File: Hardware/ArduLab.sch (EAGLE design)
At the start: 92 parts, among them CN1 USB-B, CN2 JST-PH, Q1 BSS138, Q2 BSS138, U1 ATMEGA32U4-AU, U2 MIC5205, U3 PAM2401, U4 MCP73831, U5 L293DD, U6 HC_05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

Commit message: Update
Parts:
- renumbered PB1 to S3, PB2 to S4
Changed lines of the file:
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@@
 <part name="GND32" library="SparkFun" deviceset="GND" device=""/>
 <part name="P+11" library="SparkFun" deviceset="3.3V" device="" value="VCC"/>
-<part name="PB2" library="Testing" deviceset="SWITCH-MOMENTARY-2" device="SMD-4" value="Reset"/>
+<part name="S4" library="Testing" deviceset="SWITCH-MOMENTARY-2" device="SMD-4" value="Reset"/>
 <part name="JP1" library="pinhead" deviceset="PINHD-2X4" device=""/>
 <part name="C16" library="resistor" deviceset="C-US" device="C1206" value="1uF"/>
@@
 <part name="R6" library="resistor" deviceset="R-US_" device="R1206" value="330"/>
 <part name="GND17" library="SparkFun" deviceset="GND" device=""/>
-<part name="PB1" library="SparkFun-Electromechanical" deviceset="SWITCH-MOMENTARY-2" device="SMD-12MM" value="B3FS-4052P"/>
+<part name="S3" library="SparkFun-Electromechanical" deviceset="SWITCH-MOMENTARY-2" device="SMD-12MM" value="B3FS-4052P"/>
 <part name="C23" library="SparkFun" deviceset="CAP_POL" device="3528-KIT" value="100uF"/>
 <part name="C11" library="resistor" deviceset="C-US" device="C1206" value="100nF"/>
@@
 <instance part="GND32" gate="1" x="25.4" y="36.83"/>
 <instance part="P+11" gate="G$1" x="149.86" y="46.99"/>
-<instance part="PB2" gate="G$1" x="149.86" y="20.32" rot="R90"/>
+<instance part="S4" gate="G$1" x="149.86" y="20.32" rot="R90"/>
 <instance part="JP1" gate="A" x="114.3" y="41.91"/>
 <instance part="C16" gate="G$1" x="22.86" y="135.89" rot="R90"/>
@@
 <wire x1="149.86" y1="15.24" x2="149.86" y2="12.7" width="0.1524" layer="91"/>
 <pinref part="GND3" gate="1" pin="GND"/>
-<pinref part="PB2" gate="G$1" pin="1"/>
+<pinref part="S4" gate="G$1" pin="1"/>
 </segment>
 <segment>
@@
 <pinref part="R12" gate="G$1" pin="1"/>
 <wire x1="149.86" y1="25.4" x2="149.86" y2="27.94" width="0.1524" layer="91"/>
-<pinref part="PB2" gate="G$1" pin="2"/>
+<pinref part="S4" gate="G$1" pin="2"/>
 <junction x="149.86" y="27.94"/>
 <wire x1="149.86" y1="27.94" x2="149.86" y2="30.48" width="0.1524" layer="91"/>
@@
 <instance part="R6" gate="G$1" x="35.56" y="149.86" rot="R180"/>
 <instance part="GND17" gate="1" x="20.32" y="139.7"/>
-<instance part="PB1" gate="G$1" x="115.57" y="64.77" rot="R270"/>
+<instance part="S3" gate="G$1" x="115.57" y="64.77" rot="R270"/>
 <instance part="C23" gate="G$1" x="167.64" y="67.31"/>
 <instance part="C11" gate="G$1" x="157.48" y="67.31"/>
@@
 <wire x1="115.57" y1="76.2" x2="115.57" y2="69.85" width="0.1524" layer="91"/>
 <pinref part="P+3" gate="G$1" pin="3.3V"/>
-<pinref part="PB1" gate="G$1" pin="1"/>
+<pinref part="S3" gate="G$1" pin="1"/>
 </segment>
 <segment>
@@
 <net name="D16" class="0">
 <segment>
-<pinref part="PB1" gate="G$1" pin="2"/>
+<pinref part="S3" gate="G$1" pin="2"/>
 <pinref part="R15" gate="G$1" pin="2"/>
 <wire x1="115.57" y1="48.26" x2="115.57" y2="54.61" width="0.1524" layer="91"/>

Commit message: Updated
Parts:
- C22, C26: device resistor:C-USC1206 -> resistor:C-USC3216
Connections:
- net GND: now also C17.1, C21.1; no longer C17.2, C21.2
- net VOUT: now also C17.2, C21.2; no longer C17.1, C21.1
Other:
- note added: "~"
- moved on the sheet: C17, C21

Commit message: Minor SCH Updates: V1.0 label removed
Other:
- note added: "ArduLab"
- note removed: "ArduLab V1.0"
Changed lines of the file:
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@@
 <sheet>
 <plain>
-<text x="175.26" y="12.7" size="3.81" layer="94">ArduLab V1.0</text>
+<text x="175.26" y="12.7" size="3.81" layer="94">ArduLab</text>
 <text x="215.9" y="20.32" size="2.54" layer="94">Designed by J.G.Aguado</text>
 <text x="109.22" y="102.87" size="1.778" layer="96">SCK</text>
@@
 <sheet>
 <plain>
-<text x="175.26" y="12.7" size="3.81" layer="94">ArduLab V1.0</text>
+<text x="175.26" y="12.7" size="3.81" layer="94">ArduLab</text>
 <text x="215.9" y="20.32" size="2.54" layer="94">Designed by J.G.Aguado</text>
 </plain>

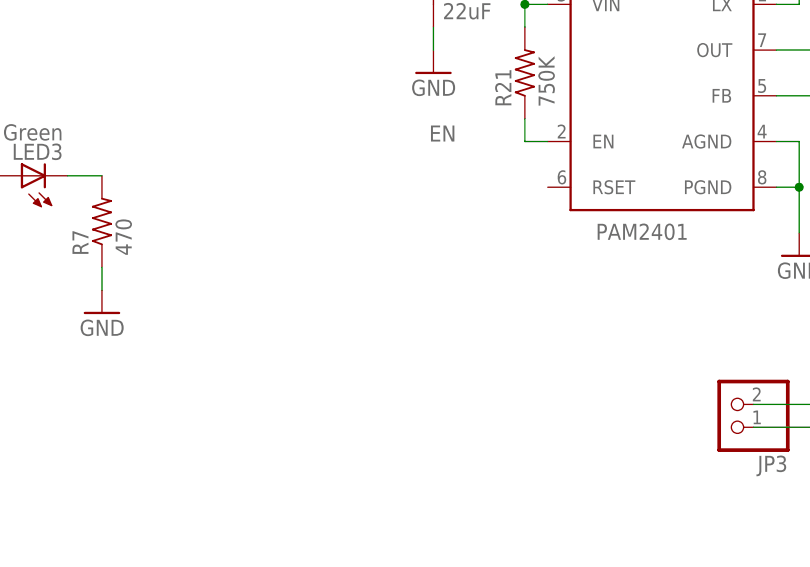
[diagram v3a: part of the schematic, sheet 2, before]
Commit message: Added R23 (100k) as optional resistor for inductor current limit
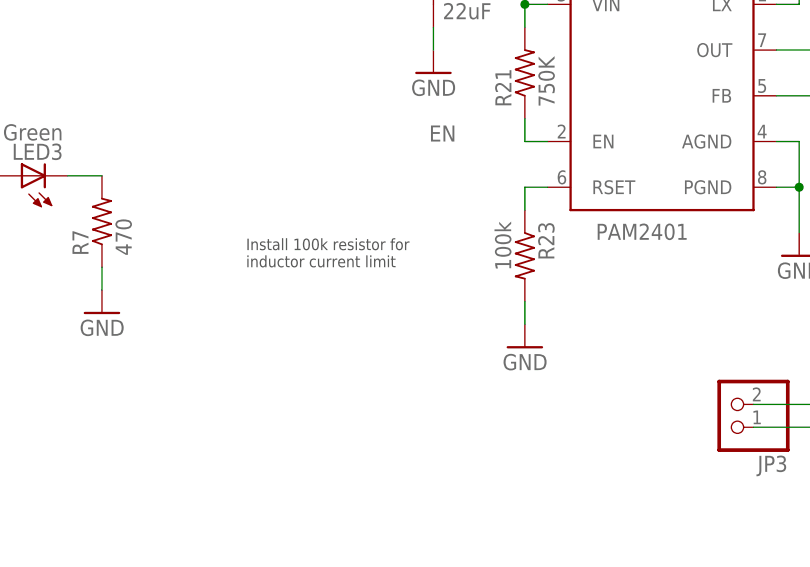
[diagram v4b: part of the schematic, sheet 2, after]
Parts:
- added R23: 100k, resistor:R-US_R1206
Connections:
- new net N$7: R23.1, U3.RSET
- net GND: now also R23.2
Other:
- note added: "Install 100k resistor for inductor current limit"
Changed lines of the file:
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@@
 <setting verticaltext="up"/>
 </settings>
-<grid distance="0.1" unitdist="inch" unit="inch" style="lines" multiple="1" display="no" altdistance="0.01" altunitdist="inch" altunit="inch"/>
+<grid distance="0.05" unitdist="inch" unit="inch" style="lines" multiple="1" display="no" altdistance="0.01" altunitdist="inch" altunit="inch"/>
 <layers>
 <layer number="1" name="Top" color="4" fill="1" visible="no" active="no"/>
@@
 <part name="U1" library="adafruit" deviceset="ATMEGA32U4" device="-AU"/>
 <part name="D3" library="diode" deviceset="DIODE-" device="SOD123" value="MBR120"/>
+<part name="R23" library="resistor" deviceset="R-US_" device="R1206" value="100k"/>
+<part name="GND5" library="SparkFun" deviceset="GND" device=""/>
 </parts>
 <sheets>
@@
 <text x="175.26" y="12.7" size="3.81" layer="94">ArduLab</text>
 <text x="215.9" y="20.32" size="2.54" layer="94">Designed by J.G.Aguado</text>
+<text x="120.142" y="119.38" size="1.27" layer="97" font="vector">Install 100k resistor for
+inductor current limit</text>
 </plain>
 <instances>
@@
 <instance part="GND13" gate="1" x="227.33" y="138.43"/>
 <instance part="D3" gate="G$1" x="80.01" y="129.54"/>
+<instance part="R23" gate="G$1" x="151.13" y="120.65" rot="R270"/>
+<instance part="GND5" gate="1" x="151.13" y="110.49" rot="MR0"/>
 </instances>
 <busses>
@@
 <pinref part="C21" gate="G$1" pin="1"/>
 <wire x1="208.28" y1="143.51" x2="208.28" y2="140.97" width="0.1524" layer="91"/>
+</segment>
+<segment>
+<pinref part="R23" gate="G$1" pin="2"/>
+<pinref part="GND5" gate="1" pin="GND"/>
+<wire x1="151.13" y1="113.03" x2="151.13" y2="115.57" width="0.1524" layer="91"/>
 </segment>
 </net>
@@
 </segment>
 </net>
+<net name="N$7" class="0">
+<segment>
+<pinref part="U3" gate="G$1" pin="RSET"/>
+<pinref part="R23" gate="G$1" pin="1"/>
+<wire x1="153.67" y1="128.27" x2="151.13" y2="128.27" width="0.1524" layer="91"/>
+<wire x1="151.13" y1="128.27" x2="151.13" y2="125.73" width="0.1524" layer="91"/>
+</segment>
+</net>
 </nets>
 </sheet>
@@
 </schematic>
 </drawing>
+<compatibility>
+<note version="6.3" minversion="6.2.2" severity="warning">
+Since Version 6.2.2 text objects can contain more than one line,
+which will not be processed correctly with this version.
+</note>
+</compatibility>
 </eagle>

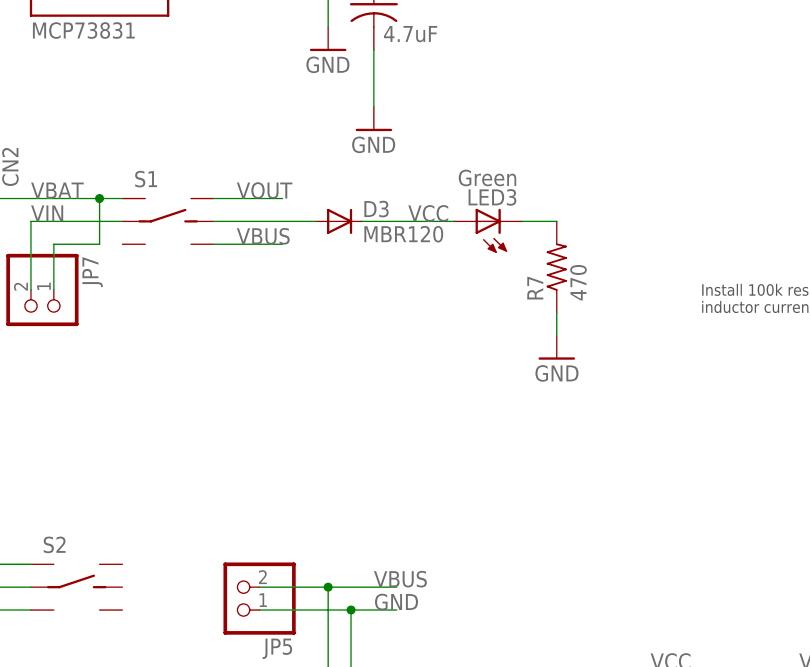
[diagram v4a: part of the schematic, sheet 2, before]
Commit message: Added PTC reset fuse 6V 500mA. Package 1206. Part number: 1206L050YR
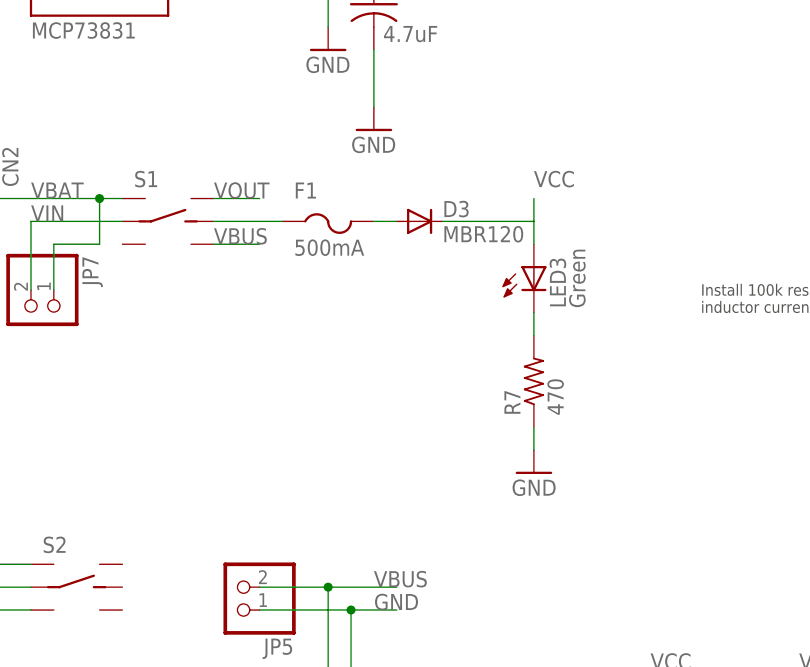
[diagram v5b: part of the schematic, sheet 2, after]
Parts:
- added F1: 500mA, adafruit:PTCFUSE-1206
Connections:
- new net N$15: D3.A, F1.2
- net N$3: now also F1.1; no longer D3.A
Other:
- moved on the sheet: D3, LED3, R7
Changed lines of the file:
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@@
 <setting verticaltext="up"/>
 </settings>
-<grid distance="0.05" unitdist="inch" unit="inch" style="lines" multiple="1" display="no" altdistance="0.01" altunitdist="inch" altunit="inch"/>
+<grid distance="0.1" unitdist="inch" unit="inch" style="lines" multiple="1" display="no" altdistance="0.01" altunitdist="inch" altunit="inch"/>
 <layers>
 <layer number="1" name="Top" color="4" fill="1" visible="no" active="no"/>
@@
 <part name="R23" library="resistor" deviceset="R-US_" device="R1206" value="100k"/>
 <part name="GND5" library="SparkFun" deviceset="GND" device=""/>
+<part name="F1" library="adafruit" deviceset="PTCFUSE" device="-1206" value="500mA"/>
 </parts>
 <sheets>
@@
 <instance part="GND12" gate="1" x="198.12" y="138.43" rot="MR0"/>
 <instance part="GND14" gate="1" x="208.28" y="138.43" rot="MR0"/>
-<instance part="GND15" gate="1" x="104.14" y="114.3" rot="MR0"/>
+<instance part="GND15" gate="1" x="101.6" y="101.6" rot="MR0"/>
 <instance part="U3" gate="G$1" x="166.37" y="138.43" smashed="yes">
 <attribute name="NAME" x="161.29" y="152.654" size="1.778" layer="95"/>
@@
 <instance part="D1" gate="G$1" x="218.44" y="148.59" rot="R90"/>
 <instance part="D2" gate="G$1" x="227.33" y="148.59" rot="R90"/>
-<instance part="R7" gate="G$1" x="104.14" y="124.46" rot="R90"/>
+<instance part="R7" gate="G$1" x="101.6" y="111.76" rot="R90"/>
 <instance part="R21" gate="G$1" x="151.13" y="140.97" rot="R90"/>
 <instance part="L1" gate="G$1" x="166.37" y="156.21" rot="R90"/>
@@
 <instance part="C17" gate="G$1" x="198.12" y="146.05" rot="R180"/>
 <instance part="C21" gate="G$1" x="208.28" y="146.05" rot="R180"/>
-<instance part="LED3" gate="G$1" x="95.25" y="129.54" rot="R90"/>
+<instance part="LED3" gate="G$1" x="101.6" y="124.46"/>
 <instance part="GND13" gate="1" x="227.33" y="138.43"/>
-<instance part="D3" gate="G$1" x="80.01" y="129.54"/>
+<instance part="D3" gate="G$1" x="88.9" y="129.54"/>
 <instance part="R23" gate="G$1" x="151.13" y="120.65" rot="R270"/>
 <instance part="GND5" gate="1" x="151.13" y="110.49" rot="MR0"/>
+<instance part="F1" gate="G$1" x="78.74" y="127"/>
 </instances>
 <busses>
@@
 <pinref part="GND15" gate="1" pin="GND"/>
 <pinref part="R7" gate="G$1" pin="1"/>
-<wire x1="104.14" y1="116.84" x2="104.14" y2="119.38" width="0.1524" layer="91"/>
+<wire x1="101.6" y1="104.14" x2="101.6" y2="106.68" width="0.1524" layer="91"/>
 </segment>
 <segment>
@@
 </segment>
 <segment>
-<wire x1="82.55" y1="129.54" x2="92.71" y2="129.54" width="0.1524" layer="91"/>
-<label x="87.63" y="129.54" size="1.778" layer="95"/>
+<wire x1="91.44" y1="129.54" x2="101.6" y2="129.54" width="0.1524" layer="91"/>
+<label x="101.6" y="133.35" size="1.778" layer="95"/>
 <pinref part="LED3" gate="G$1" pin="A"/>
 <pinref part="D3" gate="G$1" pin="C"/>
+<wire x1="101.6" y1="129.54" x2="101.6" y2="127" width="0.1524" layer="91"/>
+<wire x1="101.6" y1="129.54" x2="101.6" y2="132.08" width="0.1524" layer="91"/>
 </segment>
 </net>
@@
 <segment>
 <pinref part="S1" gate="G$1" pin="R1"/>
-<wire x1="66.04" y1="132.08" x2="73.66" y2="132.08" width="0.1524" layer="91"/>
-<label x="68.58" y="132.08" size="1.778" layer="95"/>
+<wire x1="66.04" y1="132.08" x2="71.12" y2="132.08" width="0.1524" layer="91"/>
+<label x="66.04" y="132.08" size="1.778" layer="95"/>
 </segment>
 <segment>
@@
 <segment>
 <pinref part="S1" gate="G$1" pin="R2"/>
-<wire x1="73.66" y1="127" x2="66.04" y2="127" width="0.1524" layer="91"/>
-<label x="68.58" y="127" size="1.778" layer="95"/>
+<wire x1="71.12" y1="127" x2="66.04" y2="127" width="0.1524" layer="91"/>
+<label x="66.04" y="127" size="1.778" layer="95"/>
 </segment>
 </net>
@@
 <pinref part="R7" gate="G$1" pin="2"/>
 <pinref part="LED3" gate="G$1" pin="C"/>
-<wire x1="104.14" y1="129.54" x2="100.33" y2="129.54" width="0.1524" layer="91"/>
+<wire x1="101.6" y1="116.84" x2="101.6" y2="119.38" width="0.1524" layer="91"/>
 </segment>
 </net>
 <net name="N$3" class="0">
 <segment>
-<pinref part="D3" gate="G$1" pin="A"/>
 <pinref part="S1" gate="G$1" pin="RC"/>
-<wire x1="77.47" y1="129.54" x2="66.04" y2="129.54" width="0.1524" layer="91"/>
+<pinref part="F1" gate="G$1" pin="1"/>
+<wire x1="73.66" y1="129.54" x2="66.04" y2="129.54" width="0.1524" layer="91"/>
 </segment>
 </net>
@@
 </segment>
 </net>
+<net name="N$15" class="0">
+<segment>
+<pinref part="D3" gate="G$1" pin="A"/>
+<wire x1="86.36" y1="129.54" x2="83.82" y2="129.54" width="0.1524" layer="91"/>
+<pinref part="F1" gate="G$1" pin="2"/>
+</segment>
+</net>

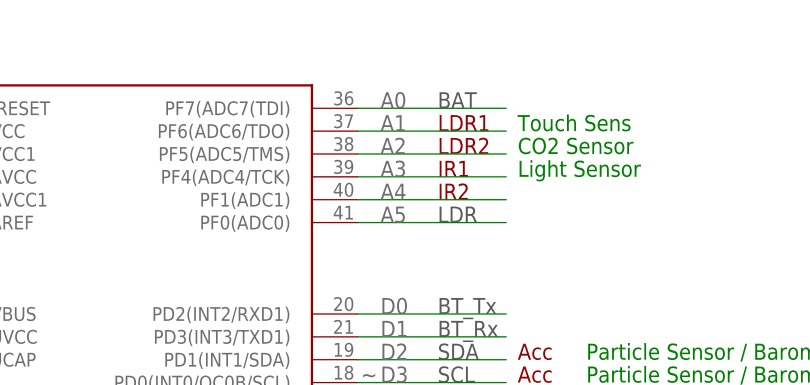
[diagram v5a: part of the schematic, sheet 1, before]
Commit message: Connection between pin A0 and battery voltage pin for monitoring the battery status.
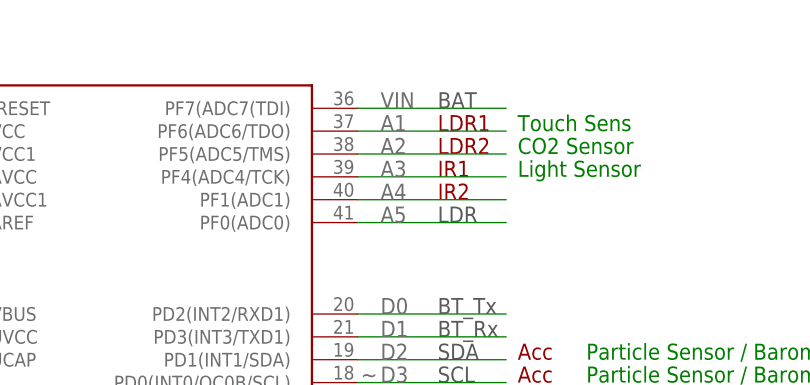
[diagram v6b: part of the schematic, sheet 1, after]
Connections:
- removed net A0: U1.PF7(ADC7(TDI)
- net VIN: now also U1.PF7(ADC7(TDI)
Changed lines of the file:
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@@
 </segment>
 </net>
-<net name="A0" class="0">
+<net name="VIN" class="0">
 <segment>
 <wire x1="90.17" y1="163.83" x2="106.68" y2="163.83" width="0.1524" layer="91"/>
